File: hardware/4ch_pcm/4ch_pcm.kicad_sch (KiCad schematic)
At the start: 5 parts, among them SW1 SW_DIP_x08, U1 BTS7004-1EPP, U2 MCP25625x-x-ML, U3 INA219AxDCN

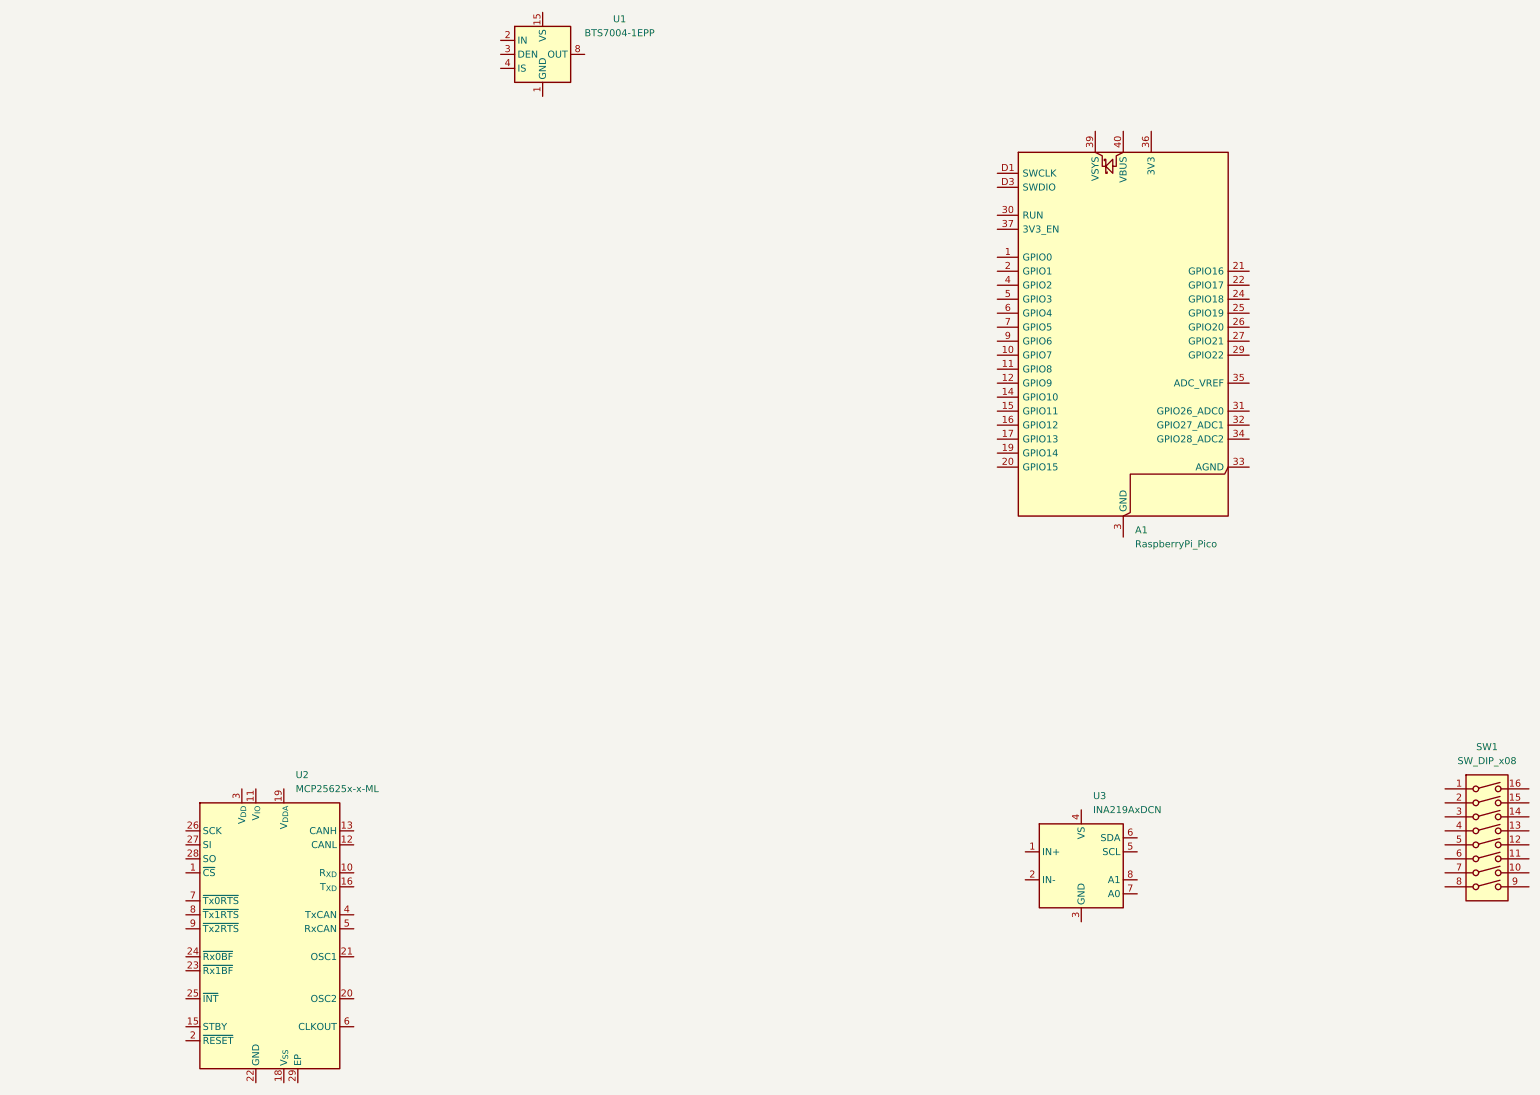
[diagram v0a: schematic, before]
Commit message: Add autosave file for 4-channel PCM schematic
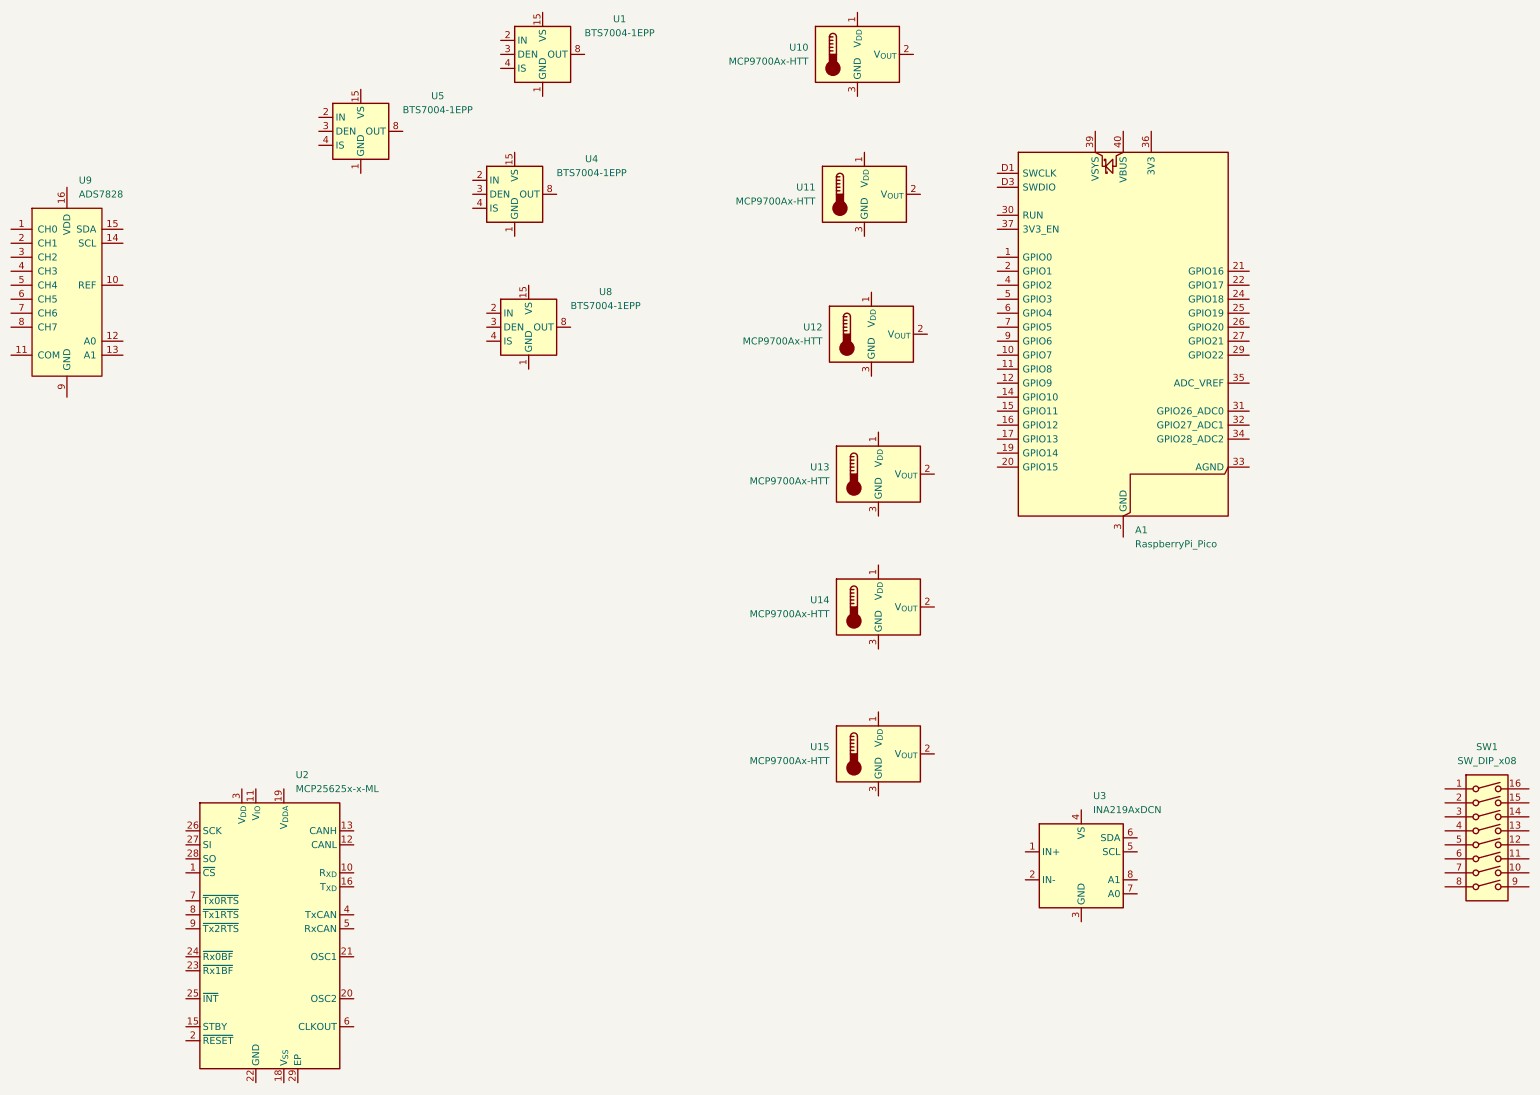
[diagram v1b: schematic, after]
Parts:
- added U10, U11, U12, U13, U14, U15: MCP9700Ax-HTT, Package_TO_SOT_SMD:SOT-23, symbol Sensor_Temperature:MCP9700Ax-HTT
- added U4, U5, U8: BTS7004-1EPP, Package_SO:Infineon_PG-TSDSO-14-22, symbol Power_Management:BTS7004-1EPP
- added U9: ADS7828, Package_SO:TSSOP-16_4.4x5mm_P0.65mm, symbol Analog_ADC:ADS7828
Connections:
- new net: U8.10 (OUT), U8.12 (OUT), U8.13 (OUT), U8.14 (OUT), U8.8 (OUT), U8.9 (OUT)
- new net: U4.10 (OUT), U4.12 (OUT), U4.13 (OUT), U4.14 (OUT), U4.8 (OUT), U4.9 (OUT)
- new net: U5.10 (OUT), U5.12 (OUT), U5.13 (OUT), U5.14 (OUT), U5.8 (OUT), U5.9 (OUT)

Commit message: save kicad
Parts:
- removed U11, U12, U13, U14: MCP9700Ax-HTT, Package_TO_SOT_SMD:SOT-23, symbol Sensor_Temperature:MCP9700Ax-HTT
- added U11, U12, U13, U14, U6, U7: MCP9700Ax-HLT, Package_TO_SOT_SMD:SOT-353_SC-70-5, symbol Sensor_Temperature:MCP9700Ax-HLT
